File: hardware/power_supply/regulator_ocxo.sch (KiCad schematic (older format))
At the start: 45 parts

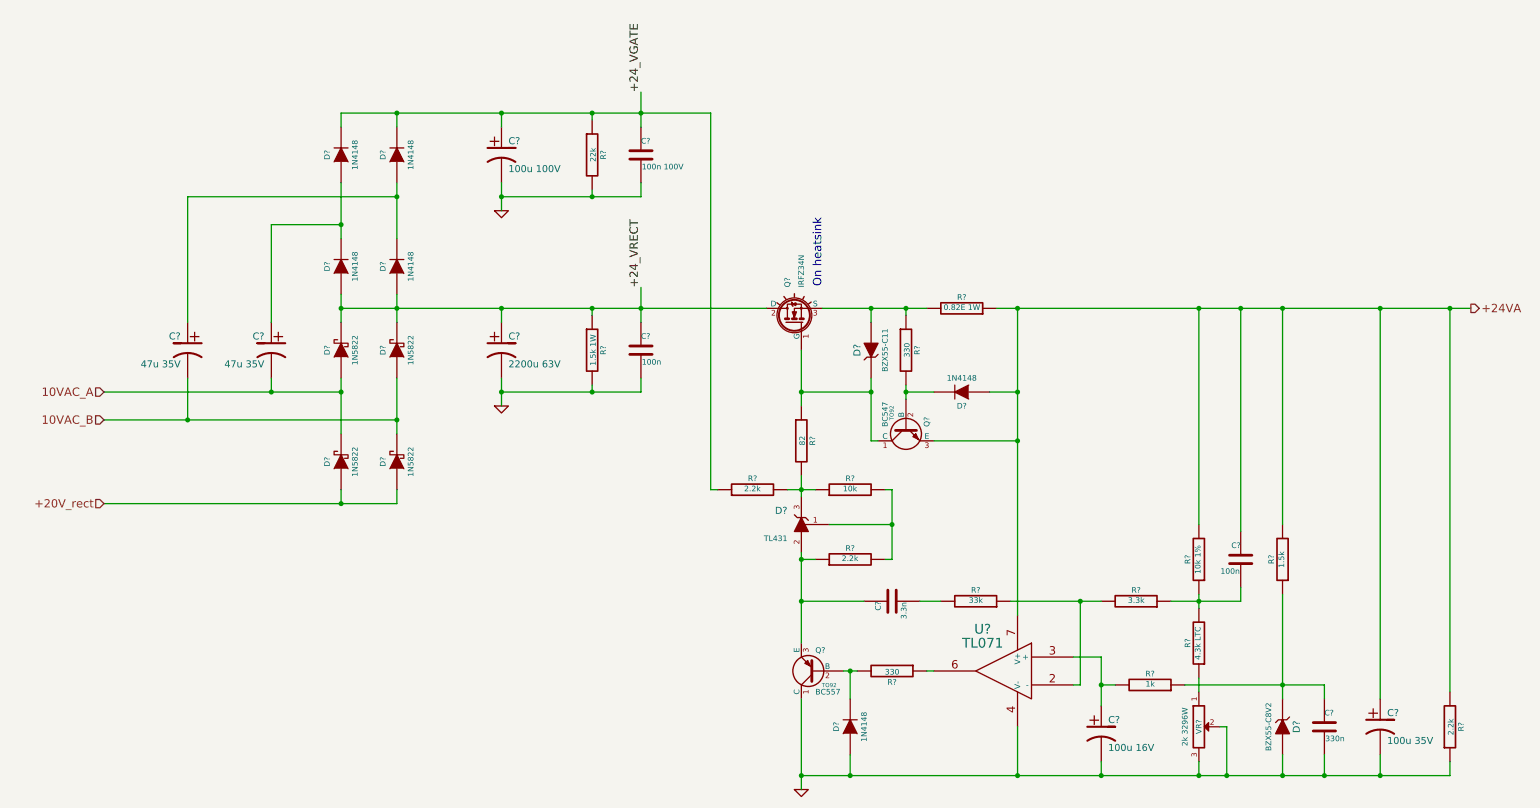
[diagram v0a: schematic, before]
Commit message: Update: PCB, schematic fixes -Almost completed power supply PCB -Removed discharge resistors from +-15, +24V supplies: no place on PCB for them -Removed ceramic capacitors (stayed in parallel with electrolytic caps): no reason for them
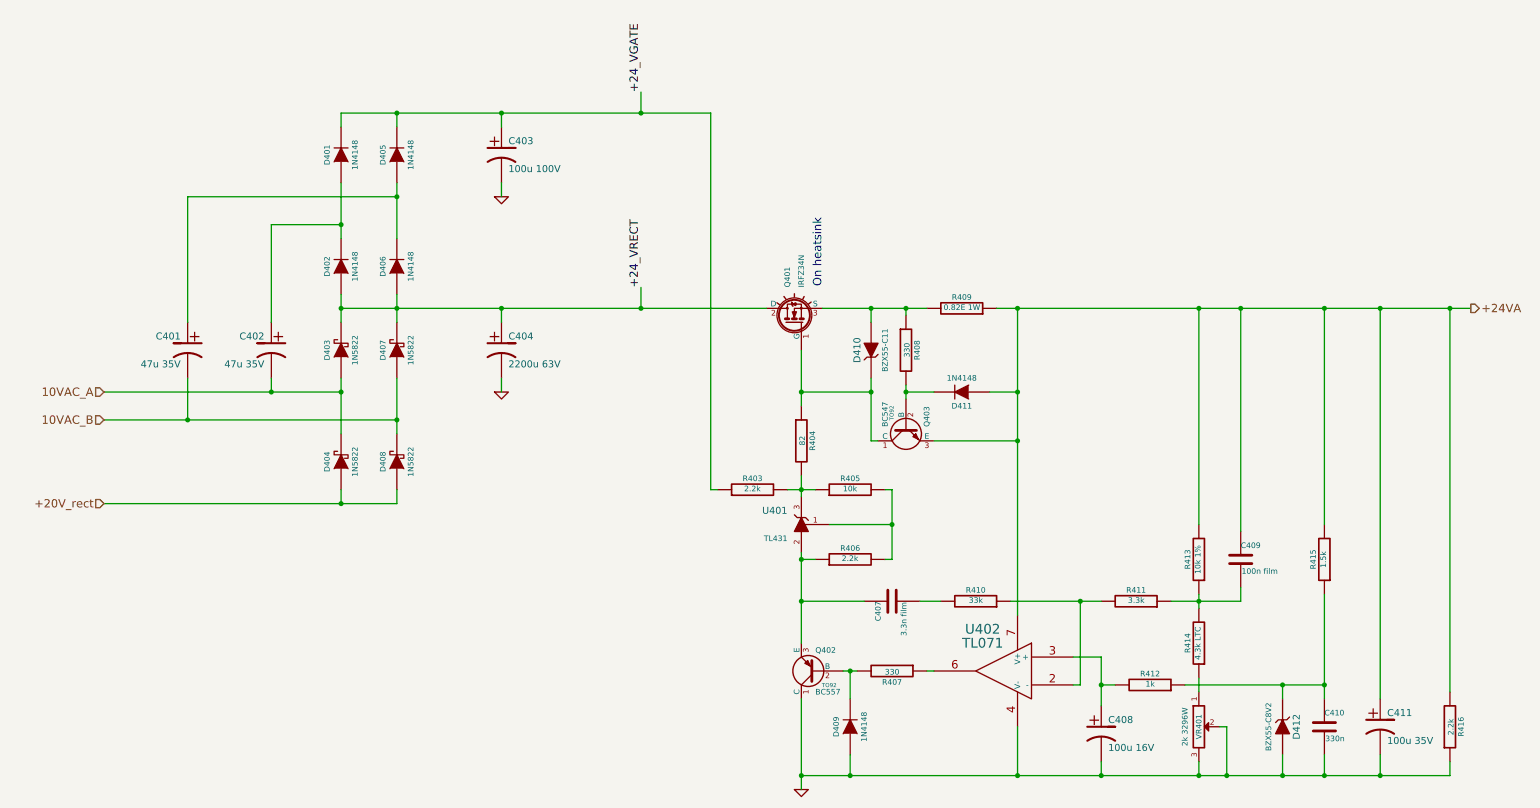
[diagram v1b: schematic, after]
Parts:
- removed C?: 100n, symbol C
- removed C?: 100n 100V, symbol C
- removed D?: TL431, TO92, symbol TL431
- removed R?: 1.5k 1W, symbol R
- removed R?: 22k, symbol R
- added U401: TL431, TO92, symbol TL431
- C407: renamed from C?; value 3.3n -> 3.3n film
- C409: renamed from C?; value 100n -> 100n film
- gave numbers to parts that had none: 38
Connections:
- net at C407.1, Q402.3 (E), R406.1: now also U401.2 (A)
- net at R405.2, R406.2: now also U401.1 (Ref)
- net at R403.2, R404.2, R405.1: now also U401.3 (K)
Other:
- moved on the sheet: R415

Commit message: Update: PCB gerbers, images. Tagged v0.15
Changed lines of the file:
@@
 $EndComp
 Wire Wire Line
-	1100 3500 2300 3500
-Wire Wire Line
-	2300 3500 2800 3500
-Wire Wire Line
-	2800 3400 2800 3500
-Wire Wire Line
-	2800 3500 2800 3800
+	1100 3500 2800 3500
+Wire Wire Line
+	2800 3400 2800 3800
 Connection ~ 2800 3500
 Wire Wire Line
-	1100 3700 1700 3700
-Wire Wire Line
-	1700 3700 3200 3700
-Wire Wire Line
-	3200 3400 3200 3700
-Wire Wire Line
-	3200 3700 3200 3800
+	1100 3700 3200 3700
+Wire Wire Line
+	3200 3400 3200 3800
 Connection ~ 3200 3700
 Connection ~ 2300 3500
@@
 	3950 2000 3950 2100
 Wire Wire Line
-	2800 2900 3200 2900
-Wire Wire Line
-	3200 2900 3950 2900
-Wire Wire Line
-	3950 2900 4950 2900
-Wire Wire Line
-	4950 2900 5850 2900
+	2800 2900 5850 2900
 Wire Wire Line
 	3950 2900 3950 3000
 Connection ~ 2800 4300
 Wire Wire Line
-	1100 4300 2800 4300
-Wire Wire Line
-	2800 4300 3200 4300
-Wire Wire Line
-	6100 6250 6450 6250
-Wire Wire Line
-	6450 6250 7650 6250
-Wire Wire Line
-	7650 6250 8250 6250
-Wire Wire Line
-	8250 6250 8950 6250
-Wire Wire Line
-	8950 6250 9150 6250
-Wire Wire Line
-	9150 6250 9550 6250
-Wire Wire Line
-	9550 6250 9850 6250
-Wire Wire Line
-	9850 6250 10250 6250
-Wire Wire Line
-	10250 6250 10750 6250
+	1100 4300 3200 4300
+Wire Wire Line
+	6100 6250 10750 6250
 $Comp
 L GND #PWR021
@@
 +24VA
 Wire Wire Line
-	6400 5500 6450 5500
-Wire Wire Line
-	6450 5500 6500 5500
+	6400 5500 6500 5500
 Wire Wire Line
 	6450 5700 6450 5500
@@
 	6950 5000 7100 5000
 Wire Wire Line
-	7600 5000 8100 5000
-Wire Wire Line
-	8100 5000 8250 5000
+	7600 5000 8250 5000
 Wire Wire Line
 	8100 5000 8100 5600
@@
 Connection ~ 8100 5000
 Wire Wire Line
-	8750 5000 8950 5000
-Wire Wire Line
-	8950 5000 9250 5000
+	8750 5000 9250 5000
 Wire Wire Line
 	9250 5000 9250 4900
 Wire Wire Line
-	8950 4950 8950 5000
-Wire Wire Line
-	8950 5000 8950 5050
+	8950 4950 8950 5050
 Connection ~ 8950 5000
 Wire Wire Line
@@
 Connection ~ 6100 4200
 Wire Wire Line
-	6250 2900 6600 2900
-Wire Wire Line
-	6600 2900 6850 2900
-Wire Wire Line
-	6850 2900 7000 2900
+	6250 2900 7000 2900
 Wire Wire Line
 	6700 4200 6750 4200
 Wire Wire Line
-	6750 4200 6750 4450
-Wire Wire Line
-	6750 4450 6750 4700
+	6750 4200 6750 4700
 Wire Wire Line
 	6750 4700 6700 4700
@@
 Connection ~ 6750 4450
 Wire Wire Line
-	7500 2900 7650 2900
-Wire Wire Line
-	7650 2900 8950 2900
-Wire Wire Line
-	8950 2900 9250 2900
-Wire Wire Line
-	9250 2900 9850 2900
-Wire Wire Line
-	9850 2900 10250 2900
-Wire Wire Line
-	10250 2900 10750 2900
-Wire Wire Line
-	10750 2900 10900 2900
-Wire Wire Line
-	7650 2900 7650 3500
-Wire Wire Line
-	7650 3500 7650 3850
-Wire Wire Line
-	7650 3850 7650 5100
+	7500 2900 10900 2900
+Wire Wire Line
+	7650 2900 7650 5100
 Wire Wire Line
 	8950 2900 8950 4450
@@
 Connection ~ 9250 2900
 Wire Wire Line
-	9850 4950 9850 5600
-Wire Wire Line
-	9850 5600 9850 5700
+	9850 4950 9850 5700
 Wire Wire Line
 	9550 6250 9550 6100
@@
 	8050 5400 8250 5400
 Wire Wire Line
-	8250 5400 8250 5600
-Wire Wire Line
-	8250 5600 8250 5750
+	8250 5400 8250 5750
 Wire Wire Line
 	8350 5600 8250 5600
 Connection ~ 8250 5600
 Wire Wire Line
-	9850 5600 9550 5600
-Wire Wire Line
-	9550 5600 8850 5600
+	8850 5600 9850 5600
 Connection ~ 9850 5600
 Connection ~ 8250 6250
@@
 Connection ~ 9550 6250
 Wire Wire Line
-	6100 4100 6100 4200
-Wire Wire Line
-	6100 4200 6100 4250
+	6100 4100 6100 4250
 Wire Wire Line
 	6600 3000 6600 2900
 Connection ~ 6600 2900
 Wire Wire Line
-	6600 3400 6600 3500
-Wire Wire Line
-	6600 3500 6600 3850
+	6600 3400 6600 3850
 Wire Wire Line
 	6600 3500 6100 3500
@@
 Connection ~ 6850 2900
 Wire Wire Line
-	6850 3450 6850 3500
-Wire Wire Line
-	6850 3500 6850 3550
+	6850 3450 6850 3550
 Wire Wire Line
 	7050 3850 7650 3850
 Connection ~ 7650 3850
 Wire Wire Line
-	6100 3200 6100 3500
-Wire Wire Line
-	6100 3500 6100 3600
+	6100 3200 6100 3600
 Wire Wire Line
 	6600 3850 6650 3850
 Connection ~ 6600 3500
 Wire Wire Line
-	6100 4650 6100 4700
-Wire Wire Line
-	6100 4700 6100 5000
-Wire Wire Line
-	6100 5000 6100 5300
-Wire Wire Line
-	6000 4200 6100 4200
-Wire Wire Line
-	6100 4200 6200 4200
+	6100 4650 6100 5300
+Wire Wire Line
+	6000 4200 6200 4200
 Connection ~ 6100 3500
 Connection ~ 9850 6250
@@
 Connection ~ 7650 6250
 Wire Wire Line
-	6100 5700 6100 6250
-Wire Wire Line
-	6100 6250 6100 6350
+	6100 5700 6100 6350
 Wire Wire Line
 	6450 6100 6450 6250
@@
 Connection ~ 4950 2900
 Wire Wire Line
-	2800 2800 2800 2900
-Wire Wire Line
-	2800 2900 2800 3000
-Wire Wire Line
-	3200 2800 3200 2900
-Wire Wire Line
-	3200 2900 3200 3000
+	2800 2800 2800 3000
+Wire Wire Line
+	3200 2800 3200 3000
 Connection ~ 2800 2900
 Wire Wire Line
-	2800 2000 2800 2300
-Wire Wire Line
-	2800 2300 2800 2400
-Wire Wire Line
-	3200 2000 3200 2100
-Wire Wire Line
-	3200 2100 3200 2400
+	2800 2000 2800 2400
+Wire Wire Line
+	3200 2000 3200 2400
 Wire Wire Line
 	3200 1600 3200 1500
 Wire Wire Line
-	2800 1500 3200 1500
-Wire Wire Line
-	3200 1500 3950 1500
-Wire Wire Line
-	3950 1500 4950 1500
-Wire Wire Line
-	4950 1500 5450 1500
+	2800 1500 5450 1500
 Wire Wire Line
 	2800 1500 2800 1600

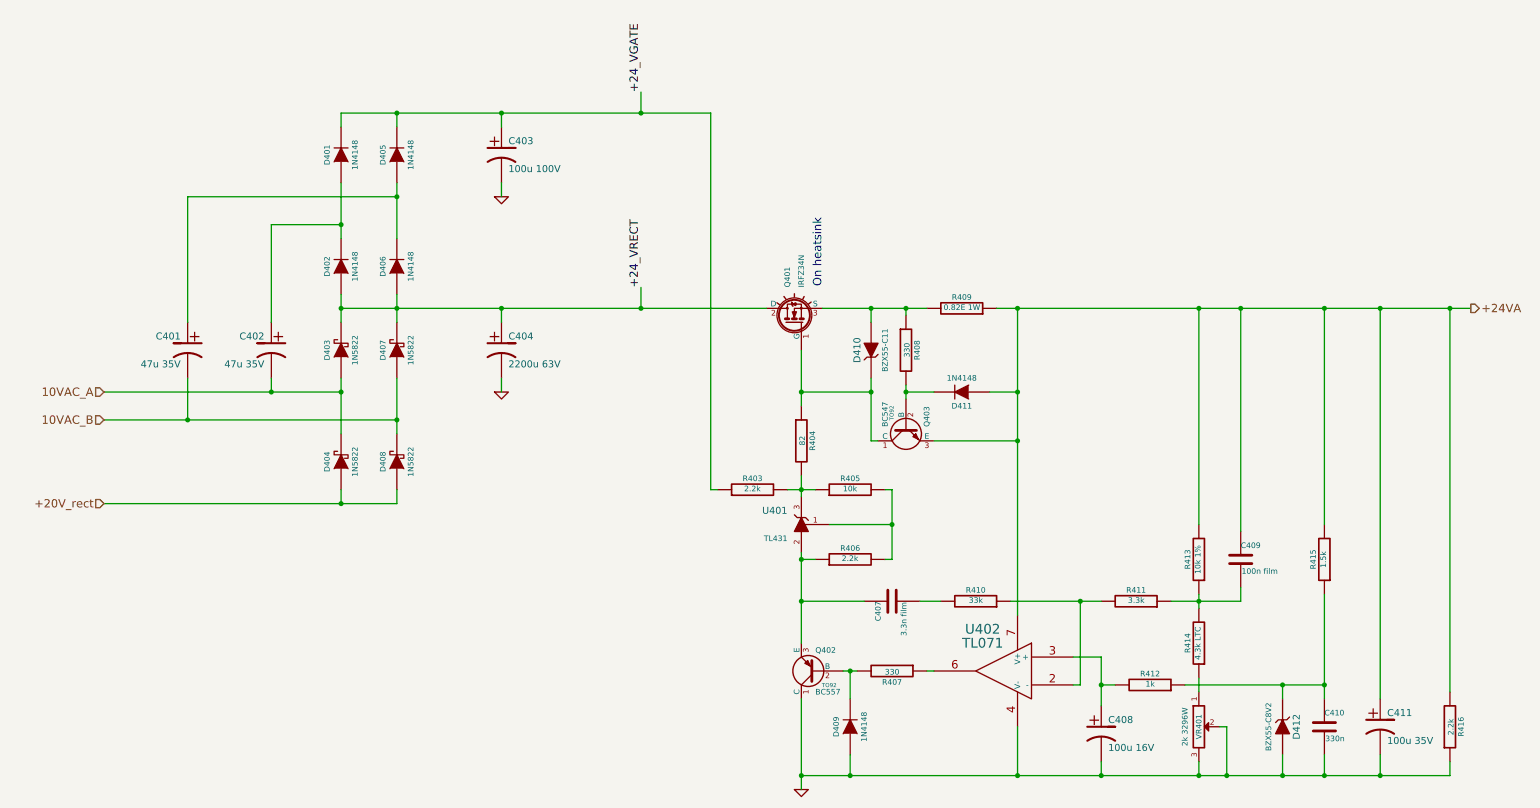
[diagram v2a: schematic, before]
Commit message: Update: fix schematic overlapping with page frame, add schematic in PDF
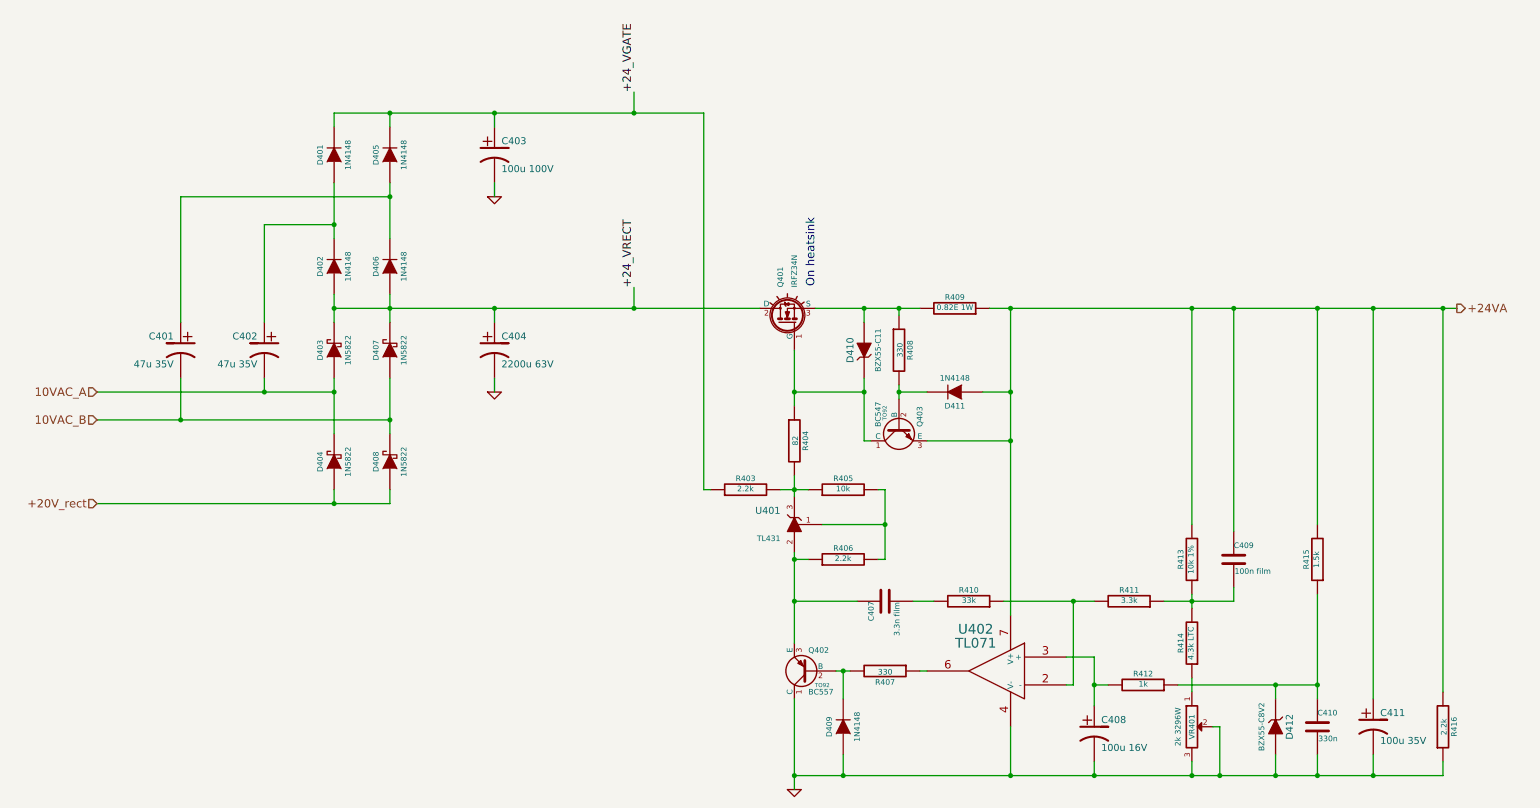
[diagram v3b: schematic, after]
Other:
- moved on the sheet: C401, C402, C403, C404, C407, C408, C409, C410, C411, D401, D402, D403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
